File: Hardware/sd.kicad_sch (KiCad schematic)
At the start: 6 parts, among them J9 ST1W008S4TR2000, Q2 PMOS

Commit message: 2nd review of schematic
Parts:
- renumbered C66 to C82, J9 to J7, JP18 to JP16, R60 to R69, R61 to R70
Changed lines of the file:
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@@
 		(on_board yes)
 		(dnp no)
-		(property "Reference" "JP18"
+		(property "Reference" "JP16"
 			(at 87.63 70.612 0)
 			(effects
@@
 			(project "RicardoTemplate"
 				(path "/7db990e4-92e1-4f99-b4d2-435bbec1ba83/b3c2f461-38d3-4d4d-a4e6-b155780b2822"
-					(reference "JP18")
+					(reference "JP16")
 					(unit 1)
 				)
@@
 		(on_board yes)
 		(dnp no)
-		(property "Reference" "C66"
+		(property "Reference" "C82"
 			(at 96.266 79.248 0)
 			(effects
@@
 			(project "RicardoTemplate"
 				(path "/7db990e4-92e1-4f99-b4d2-435bbec1ba83/b3c2f461-38d3-4d4d-a4e6-b155780b2822"
-					(reference "C66")
+					(reference "C82")
 					(unit 1)
 				)
@@
 		(on_board yes)
 		(dnp no)
-		(property "Reference" "#PWR0127"
+		(property "Reference" "#PWR0144"
 			(at 105.156 95.758 0)
 			(effects
@@
 			(project "RicardoTemplate"
 				(path "/7db990e4-92e1-4f99-b4d2-435bbec1ba83/b3c2f461-38d3-4d4d-a4e6-b155780b2822"
-					(reference "#PWR0127")
+					(reference "#PWR0144")
 					(unit 1)
 				)
@@
 		(on_board yes)
 		(dnp no)
-		(property "Reference" "#PWR0129"
+		(property "Reference" "#PWR0146"
 			(at 124.46 62.484 0)
 			(effects
@@
 			(project "RicardoTemplate"
 				(path "/7db990e4-92e1-4f99-b4d2-435bbec1ba83/b3c2f461-38d3-4d4d-a4e6-b155780b2822"
-					(reference "#PWR0129")
+					(reference "#PWR0146")
 					(unit 1)
 				)
@@
 		(dnp no)
 		(fields_autoplaced yes)
-		(property "Reference" "#PWR0126"
+		(property "Reference" "#PWR0143"
 			(at 105.156 67.564 0)
 			(effects
@@
 			(project "RicardoTemplate"
 				(path "/7db990e4-92e1-4f99-b4d2-435bbec1ba83/b3c2f461-38d3-4d4d-a4e6-b155780b2822"
-					(reference "#PWR0126")
+					(reference "#PWR0143")
 					(unit 1)
 				)
@@
 		(on_board yes)
 		(dnp no)
-		(property "Reference" "R60"
+		(property "Reference" "R69"
 			(at 110.109 73.0281 0)
 			(effects
@@
 			(project "RicardoTemplate"
 				(path "/7db990e4-92e1-4f99-b4d2-435bbec1ba83/b3c2f461-38d3-4d4d-a4e6-b155780b2822"
-					(reference "R60")
+					(reference "R69")
 					(unit 1)
 				)
@@
 		(on_board yes)
 		(dnp no)
-		(property "Reference" "R61"
+		(property "Reference" "R70"
 			(at 120.65 58.674 0)
 			(effects
@@
 			(project "RicardoTemplate"
 				(path "/7db990e4-92e1-4f99-b4d2-435bbec1ba83/b3c2f461-38d3-4d4d-a4e6-b155780b2822"
-					(reference "R61")
+					(reference "R70")
 					(unit 1)
 				)
@@
 		(dnp no)
 		(fields_autoplaced yes)
-		(property "Reference" "J9"
+		(property "Reference" "J7"
 			(at 137.922 64.9435 0)
 			(effects
@@
 			(project "RicardoTemplate"
 				(path "/7db990e4-92e1-4f99-b4d2-435bbec1ba83/b3c2f461-38d3-4d4d-a4e6-b155780b2822"
-					(reference "J9")
+					(reference "J7")
 					(unit 1)
 				)
@@
 		(dnp no)
 		(fields_autoplaced yes)
-		(property "Reference" "#PWR0128"
+		(property "Reference" "#PWR0145"
 			(at 113.538 81.788 0)
 			(effects
@@
 			(project "RicardoTemplate"
 				(path "/7db990e4-92e1-4f99-b4d2-435bbec1ba83/b3c2f461-38d3-4d4d-a4e6-b155780b2822"
-					(reference "#PWR0128")
+					(reference "#PWR0145")
 					(unit 1)
 				)
@@
 		(dnp no)
 		(fields_autoplaced yes)
-		(property "Reference" "#PWR0130"
+		(property "Reference" "#PWR0147"
 			(at 153.162 108.458 0)
 			(effects
@@
 			(project "RicardoTemplate"
 				(path "/7db990e4-92e1-4f99-b4d2-435bbec1ba83/b3c2f461-38d3-4d4d-a4e6-b155780b2822"
-					(reference "#PWR0130")
+					(reference "#PWR0147")
 					(unit 1)
 				)
@@
 		(on_board yes)
 		(dnp no)
-		(property "Reference" "#PWR051"
+		(property "Reference" "#PWR0142"
 			(at 101.346 88.138 0)
 			(effects
@@
 			(project "RicardoTemplate"
 				(path "/7db990e4-92e1-4f99-b4d2-435bbec1ba83/b3c2f461-38d3-4d4d-a4e6-b155780b2822"
-					(reference "#PWR051")
-					(unit 1)
-				)
+					(reference "#PWR0142")
+					(unit 1)
+				)

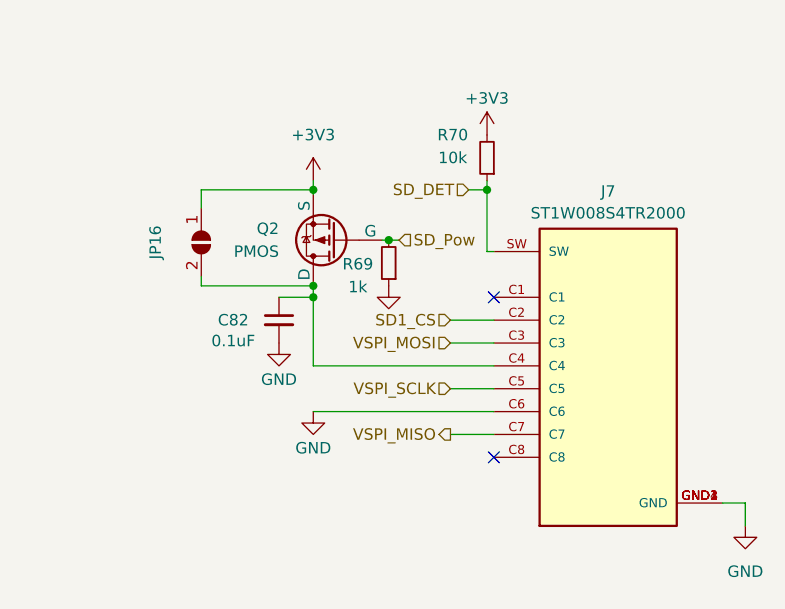
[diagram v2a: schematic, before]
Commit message: pcb and schematic update
Found all footprints including J3, pressure controller, tvs diode. PCB infrastructure update
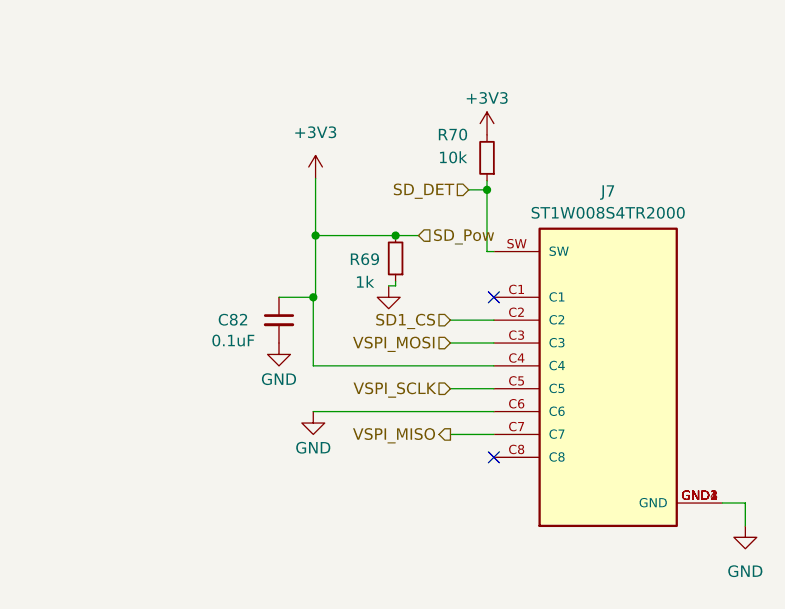
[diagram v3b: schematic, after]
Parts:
- removed JP16: SolderJumper_2_Open, iclr:SmallerSolderJP, symbol Jumper:SolderJumper_2_Open
- removed Q2: PMOS, Package_TO_SOT_SMD:SOT-23, symbol Simulation_SPICE:PMOS
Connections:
- net SD_Pow is gone; now on net +3V3: R69.2
- net +3V3: now also C82.1, J7.C4
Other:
- moved on the sheet: R69
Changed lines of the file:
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@@
 	(paper "A4")
 	(junction
-		(at 105.156 64.77)
+		(at 105.41 69.85)
 		(diameter 0)
 		(color 0 0 0 0)
 	)
 	(junction
-		(at 105.156 75.438)
-		(diameter 0)
-		(color 0 0 0 0)
-	)
-	(junction
-		(at 113.538 70.358)
+		(at 114.3 69.85)
 		(diameter 0)
 		(color 0 0 0 0)
@@
 	(wire
 		(pts
-			(xy 105.156 64.77) (xy 105.156 65.278)
-		)
-		(stroke
-			(width 0)
-			(type default)
-		)
-	)
-	(wire
-		(pts
 			(xy 120.396 79.248) (xy 125.222 79.248)
 		)
@@
 	(wire
 		(pts
-			(xy 105.156 75.438) (xy 105.156 76.708)
-		)
-		(stroke
-			(width 0)
-			(type default)
-		)
-	)
-	(wire
-		(pts
-			(xy 105.156 75.438) (xy 92.71 75.438)
+			(xy 105.41 69.85) (xy 105.41 76.708)
+		)
+		(stroke
+			(width 0)
+			(type default)
+		)
+	)
+	(wire
+		(pts
+			(xy 105.41 69.85) (xy 114.3 69.85)
+		)
+		(stroke
+			(width 0)
+			(type default)
+		)
+	)
+	(wire
+		(pts
+			(xy 105.156 76.708) (xy 105.41 76.708)
 		)
 		(stroke
@@
 	(wire
 		(pts
+			(xy 114.3 74.93) (xy 114.3 75.438)
+		)
+		(stroke
+			(width 0)
+			(type default)
+		)
+	)
+	(wire
+		(pts
 			(xy 101.346 76.708) (xy 105.156 76.708)
 		)
@@
 	(wire
 		(pts
+			(xy 114.3 75.438) (xy 113.538 75.438)
+		)
+		(stroke
+			(width 0)
+			(type default)
+		)
+	)
+	(wire
+		(pts
 			(xy 105.156 84.328) (xy 125.222 84.328)
 		)
@@
 	(wire
 		(pts
-			(xy 112.776 70.358) (xy 113.538 70.358)
-		)
-		(stroke
-			(width 0)
-			(type default)
-		)
-	)
-	(wire
-		(pts
-			(xy 92.71 64.77) (xy 105.156 64.77)
-		)
-		(stroke
-			(width 0)
-			(type default)
-		)
-	)
-	(wire
-		(pts
 			(xy 120.396 91.948) (xy 125.222 91.948)
 		)
@@
 	(wire
 		(pts
-			(xy 92.71 75.438) (xy 92.71 74.422)
+			(xy 116.84 69.85) (xy 114.3 69.85)
 		)
 		(stroke
@@
 	(wire
 		(pts
-			(xy 105.156 63.754) (xy 105.156 64.77)
-		)
-		(stroke
-			(width 0)
-			(type default)
-		)
-	)
-	(wire
-		(pts
-			(xy 113.538 70.358) (xy 114.681 70.358)
-		)
-		(stroke
-			(width 0)
-			(type default)
-		)
-	)
-	(wire
-		(pts
-			(xy 92.71 66.802) (xy 92.71 64.77)
+			(xy 105.41 63.5) (xy 105.41 69.85)
 		)
 		(stroke
@@
 	(hierarchical_label "SD_Pow"
 		(shape input)
-		(at 114.681 70.358 0)
+		(at 116.84 69.85 0)
 		(effects
 			(font
@@
 			)
 			(justify right)
-		)
-	)
-	(symbol
-		(lib_id "Jumper:SolderJumper_2_Open")
-		(at 92.71 70.612 270)
-		(unit 1)
-		(exclude_from_sim no)
-		(in_bom yes)
-		(on_board yes)
-		(dnp no)
-		(property "Reference" "JP16"
-			(at 87.63 70.612 0)
-			(effects
-				(font
-					(size 1.27 1.27)
-				)
-			)
-		)
-		(property "Value" "SolderJumper_2_Open"
-			(at 60.96 52.832 0)
-			(effects
-				(font
-					(size 1.27 1.27)
-				)
-				(hide yes)
-			)
-		)
-		(property "Footprint" "iclr:SmallerSolderJP"
-			(at 92.71 70.612 0)
-			(effects
-				(font
-					(size 1.27 1.27)
-				)
-				(hide yes)
-			)
-		)
-		(property "Datasheet" "~"
-			(at 92.71 70.612 0)
-			(effects
-				(font
-					(size 1.27 1.27)
-				)
-				(hide yes)
-			)
-		)
-		(property "Description" ""
-			(at 92.71 70.612 0)
-			(effects
-				(font
-					(size 1.27 1.27)
-				)
-				(hide yes)
-			)
-		)
-		(pin "1"
-		)
-		(pin "2"
-		)
-		(instances
-			(project "RicardoTemplate"
-				(path "/7db990e4-92e1-4f99-b4d2-435bbec1ba83/b3c2f461-38d3-4d4d-a4e6-b155780b2822"
-					(reference "JP16")
-					(unit 1)
-				)
-			)
 		)
 	)
@@
 	)
 	(symbol
-		(lib_id "Simulation_SPICE:PMOS")
-		(at 107.696 70.358 180)
-		(unit 1)
-		(exclude_from_sim no)
-		(in_bom yes)
-		(on_board yes)
-		(dnp no)
-		(fields_autoplaced yes)
-		(property "Reference" "Q2"
-			(at 101.346 69.088 0)
-			(effects
-				(font
-					(size 1.27 1.27)
-				)
-				(justify left)
-			)
-		)
-		(property "Value" "PMOS"
-			(at 101.346 71.628 0)
-			(effects
-				(font
-					(size 1.27 1.27)
-				)
-				(justify left)
-			)
-		)
-		(property "Footprint" "Package_TO_SOT_SMD:SOT-23"
-			(at 102.616 72.898 0)
-			(effects
-				(font
-					(size 1.27 1.27)
-				)
-				(hide yes)
-			)
-		)
-		(property "Datasheet" "https://ngspice.sourceforge.io/docs/ngspice-manual.pdf"
-			(at 107.696 57.658 0)
-			(effects
-				(font
-					(size 1.27 1.27)
-				)
-				(hide yes)
-			)
-		)
-		(property "Description" ""
-			(at 107.696 70.358 0)
-			(effects
-				(font
-					(size 1.27 1.27)
-				)
-				(hide yes)
-			)
-		)
-		(property "Sim.Device" "PMOS"
-			(at 107.696 53.213 0)
-			(effects
-				(font
-					(size 1.27 1.27)
-				)
-				(hide yes)
-			)
-		)
-		(property "Sim.Type" "VDMOS"
-			(at 107.696 51.308 0)
-			(effects
-				(font
-					(size 1.27 1.27)
-				)
-				(hide yes)
-			)
-		)
-		(property "Sim.Pins" "1=D 2=G 3=S"
-			(at 107.696 55.118 0)
-			(effects
-				(font
-					(size 1.27 1.27)
-				)
-				(hide yes)
-			)
-		)
-		(property "MPN" " DMP3099L"
-			(at 107.696 70.358 0)
-			(effects
-				(font
-					(size 1.27 1.27)
-				)
-				(hide yes)
-			)
-		)
-		(pin "2"
-		)
-		(pin "3"
-		)
-		(pin "1"
-		)
-		(instances
-			(project "RicardoTemplate"
-				(path "/7db990e4-92e1-4f99-b4d2-435bbec1ba83/b3c2f461-38d3-4d4d-a4e6-b155780b2822"
-					(reference "Q2")
-					(unit 1)
-				)
-			)
-		)
-	)
-	(symbol
 		(lib_id "power:+3.3V")
 		(at 124.46 58.674 0)
@@
 	(symbol
 		(lib_id "power:+3.3V")
-		(at 105.156 63.754 0)
+		(at 105.41 63.5 0)
 		(unit 1)
 		(exclude_from_sim no)
@@
 		(fields_autoplaced yes)
 		(property "Reference" "#PWR0143"
-			(at 105.156 67.564 0)
+			(at 105.41 67.31 0)
 			(effects
 				(font
@@
 		)
 		(property "Value" "+3V3"
-			(at 105.156 58.674 0)
+			(at 105.41 58.42 0)
 			(effects
 				(font
@@
 		)
 		(property "Footprint" ""
-			(at 105.156 63.754 0)
+			(at 105.41 63.5 0)
 			(effects
 				(font
@@
 		)
 		(property "Datasheet" ""
-			(at 105.156 63.754 0)
+			(at 105.41 63.5 0)
 			(effects
 				(font
@@
 		)
 		(property "Description" ""
-			(at 105.156 63.754 0)
+			(at 105.41 63.5 0)
 			(effects
 				(font
@@
 	(symbol
 		(lib_id "Device:R_Small")
-		(at 113.538 72.898 180)
+		(at 114.3 72.39 180)
 		(unit 1)
 		(exclude_from_sim no)
@@
 		(dnp no)
 		(property "Reference" "R69"
-			(at 110.109 73.0281 0)
+			(at 110.871 72.5201 0)
 			(effects
 				(font
@@
 		)
 		(property "Value" "1k"
-			(at 110.109 75.565 0)
+			(at 110.871 75.057 0)
 			(effects
 				(font
@@
 		)
 		(property "Footprint" "Resistor_SMD:R_0402_1005Metric"
-			(at 113.538 72.898 0)
+			(at 114.3 72.39 0)
 			(effects
 				(font
@@
 		)
 		(property "Datasheet" "~"
-			(at 113.538 72.898 0)
+			(at 114.3 72.39 0)
 			(effects
 				(font
@@
 		)
 		(property "Description" ""
-			(at 113.538 72.898 0)
-			(effects
-				(font
+			(at 114.3 72.39 0)
+			(effects
+				(font

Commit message: schematic changes and updated tvs footprints
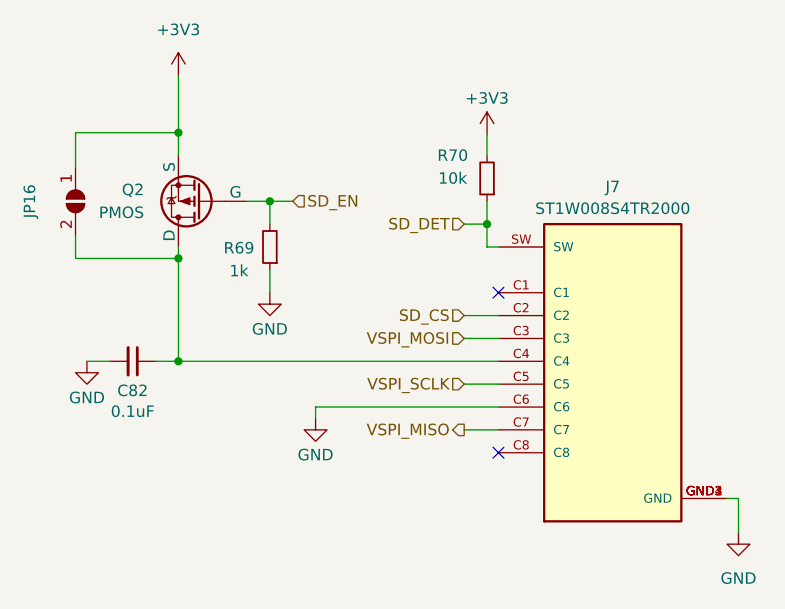
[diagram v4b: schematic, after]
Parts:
- added JP16: SolderJumper_2_Open, iclr:SmallerSolderJP, symbol Jumper:SolderJumper_2_Open
- added Q2: PMOS, Package_TO_SOT_SMD:SOT-23, symbol Simulation_SPICE:PMOS
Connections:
- net +3V3: now also JP16.1 (A), Q2.3 (S); no longer C82.1, J7.C4, R69.2
- net SD1_CS renamed SD_CS
- new net: C82.1, J7.C4, JP16.2 (B), Q2.1 (D)
- new net SD_EN: Q2.2 (G), R69.2
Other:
- moved on the sheet: C82, J7, R70
